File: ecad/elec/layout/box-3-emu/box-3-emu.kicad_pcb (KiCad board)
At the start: 2 copper layers, 72.5 x 63.9 mm, 56 parts

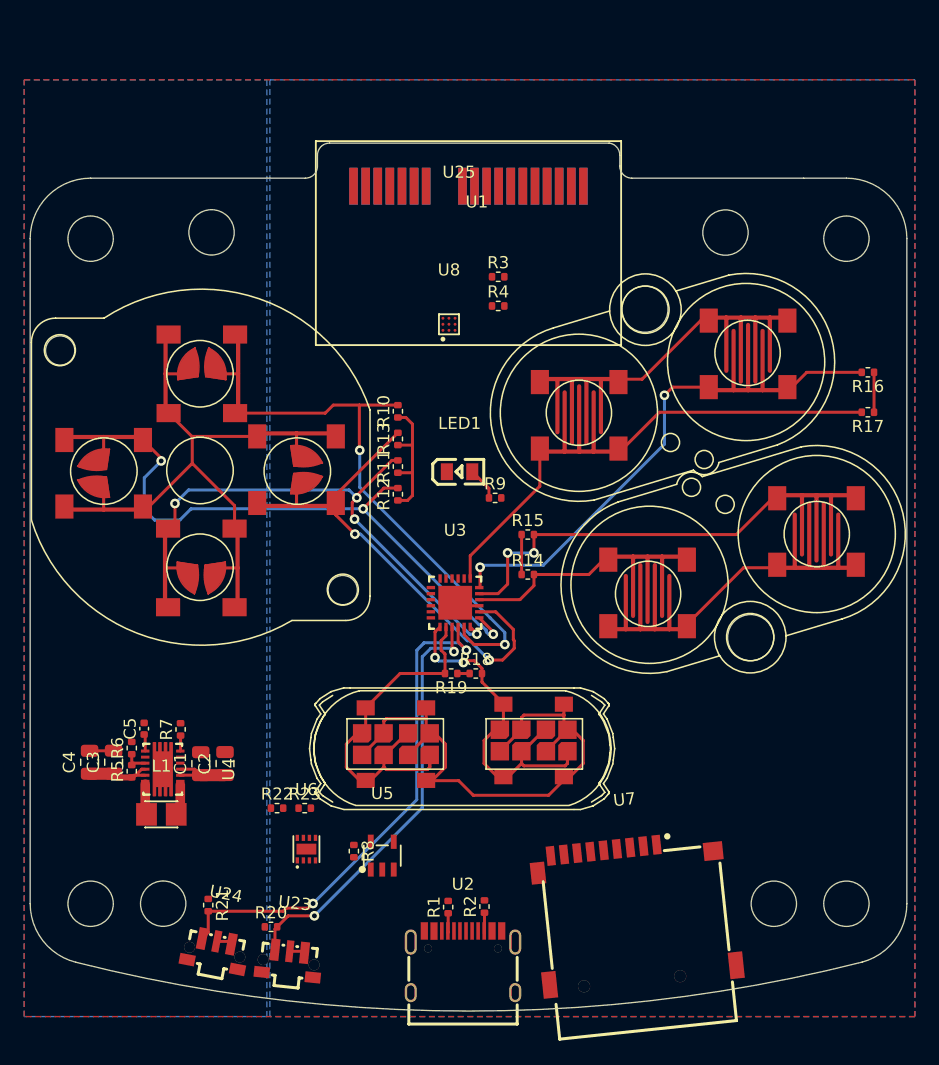
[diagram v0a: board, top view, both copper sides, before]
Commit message: update box-emu and box-3-emu borads
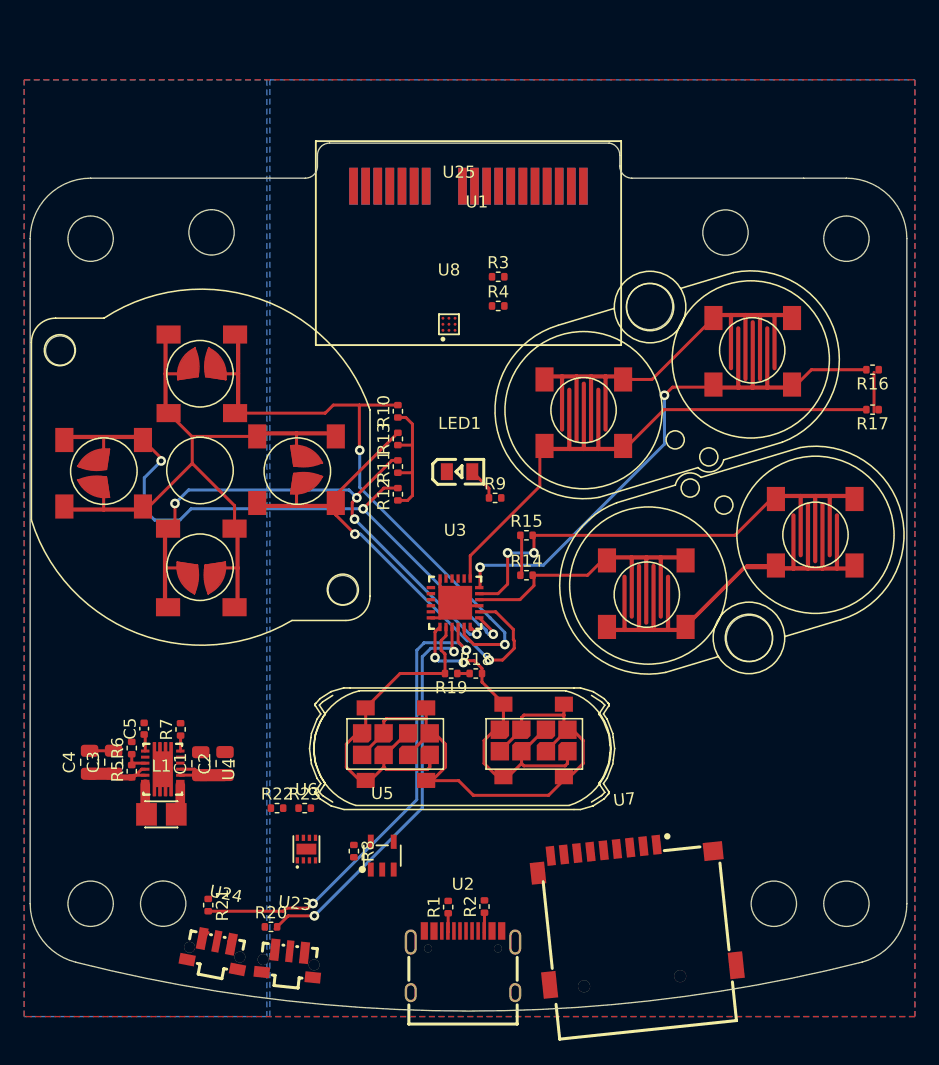
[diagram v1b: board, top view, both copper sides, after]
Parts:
- moved R16 0.44 mm to (168.9, 73.9)
- moved R17 0.44 mm to (168.9, 77.2)
- moved U18 0.44 mm to (159.0, 72.3)
- moved U19 0.44 mm to (145.0, 77.4)
- moved U17 0.44 mm to (152.0, 74.7)
- moved R14 0.12 mm to (140.3, 90.8)
- moved R15 0.12 mm to (140.3, 87.5)
- moved U14 0.12 mm to (157.2, 90.0)
- moved U15 0.12 mm to (150.2, 92.4)
- moved U16 0.12 mm to (164.1, 87.3)
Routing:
- net box-vcc: track 50.9 -> 67.8 mm
- net (no net): track 12.5 -> 0.00 mm
- net box-gnd: track 22.8 -> 27.9 mm
- net p1_3: track 42.7 -> 41.0 mm
- net p1_2: track 35.7 -> 34.0 mm

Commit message: WIP fleshing out more of the design
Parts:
- added U2: , lib:CONN-SMD_P2.00_S2B-PH-SM4-TB-LF-SN, B.Cu at (119.6, 116.7)
- R6: value 62.5mW Thick Film Resistors 50V ±100ppm/℃ ±0.5% 27.4kΩ 0402 Chip Resistor - Surface Mount ROHS -> 62.5mW Thick Film Resistors 50V ±100ppm/℃ ±1% 27.4kΩ 0402 Chip Resistor - Surface Mount ROHS
- renumbered U9 to U10, U10 to U11, U11 to U12, U12 to U13, U13 to U14, U14 to U15, U15 to U16, U16 to U17, U17 to U18, U18 to U19, U19 to U20, U20 to U21, U21 to U22, U22 to U23, U23 to U24, U24 to U25, U25 to U26, U26 to U27, U2 to U3, U3 to U4, U4 to U5, U5 to U6, U6 to U7, U7 to U8, U8 to U9
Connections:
- U24 pad 1: p1_2 -> box-vcc
- U24 pad 2: box-vcc -> p1_2
- U25 pad 1: p1_3 -> box-vcc
- U25 pad 2: box-vcc -> p1_3
- U4 pad 18: ad0 -> box-gnd
- U4 pad 24: ad1 -> box-gnd
- U9 pad A1: (no net) -> en
- U9 pad A2: (no net) -> reg
- U9 pad A3: (no net) -> out_p
- U9 pad B1: (no net) -> in_trig
- U9 pad B2: (no net) -> sda
- U9 pad B3: (no net) -> box-gnd
- U9 pad C1: (no net) -> scl
- U9 pad C2: (no net) -> box-vcc
- U9 pad C3: (no net) -> out_m
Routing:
- net p1_3: track 41.0 -> 40.3 mm
- net box-vcc: track 67.8 -> 68.5 mm

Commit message: update layouts
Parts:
- removed the U27 at (135.5, 58.7)
- added DS1: , lib:SOD-323_L1.8-W1.3-LS2.5-RD, F.Cu at (118.7, 103.5)
- added J1: , lib:CONN-SMD_4P-P1.00_SM04B-SRSS-TB-LF-SN, F.Cu at (165.7, 105.3)
- added U10: , Connector_PinHeader_1.00mm:PinHeader_1x02_P1.00mm_Vertical, F.Cu at (125.0, 65.4)
- added U28: , lib:CONN_5-1734857-1_TEC, F.Cu at (135.5, 58.7)
- moved U2 6.09 mm to (125.2, 119.1)
- renumbered U10 to U11, U11 to U12, U12 to U13, U13 to U14, U14 to U15, U15 to U16, U16 to U17, U17 to U18, U18 to U19, U19 to U20, U20 to U21, U21 to U22, U22 to U23, U23 to U24, U24 to U25, U25 to U26, U26 to U27
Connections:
- U9 pad A3: out_p -> a
- U9 pad C3: out_m -> b

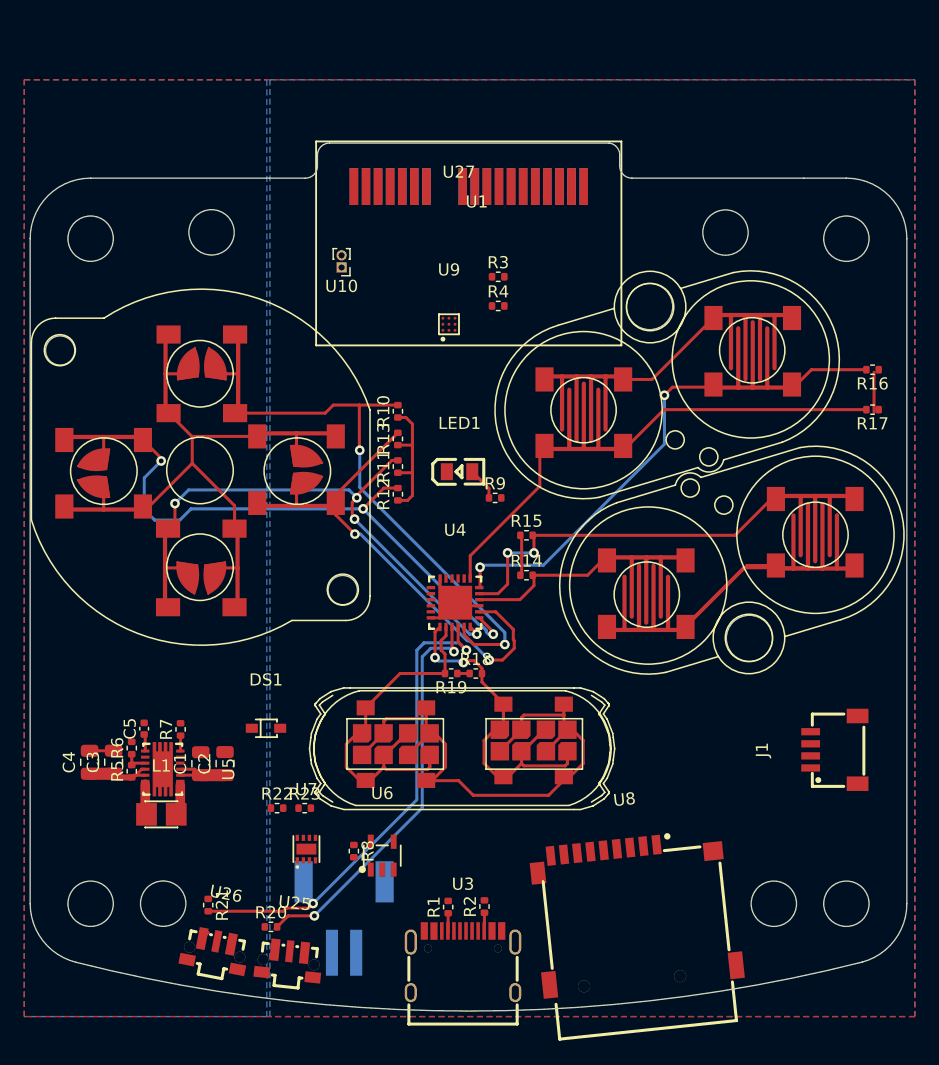
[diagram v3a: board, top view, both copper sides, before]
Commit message: change drv2605 to tssop and update box-3 connector. flesh out implemenation and wiring
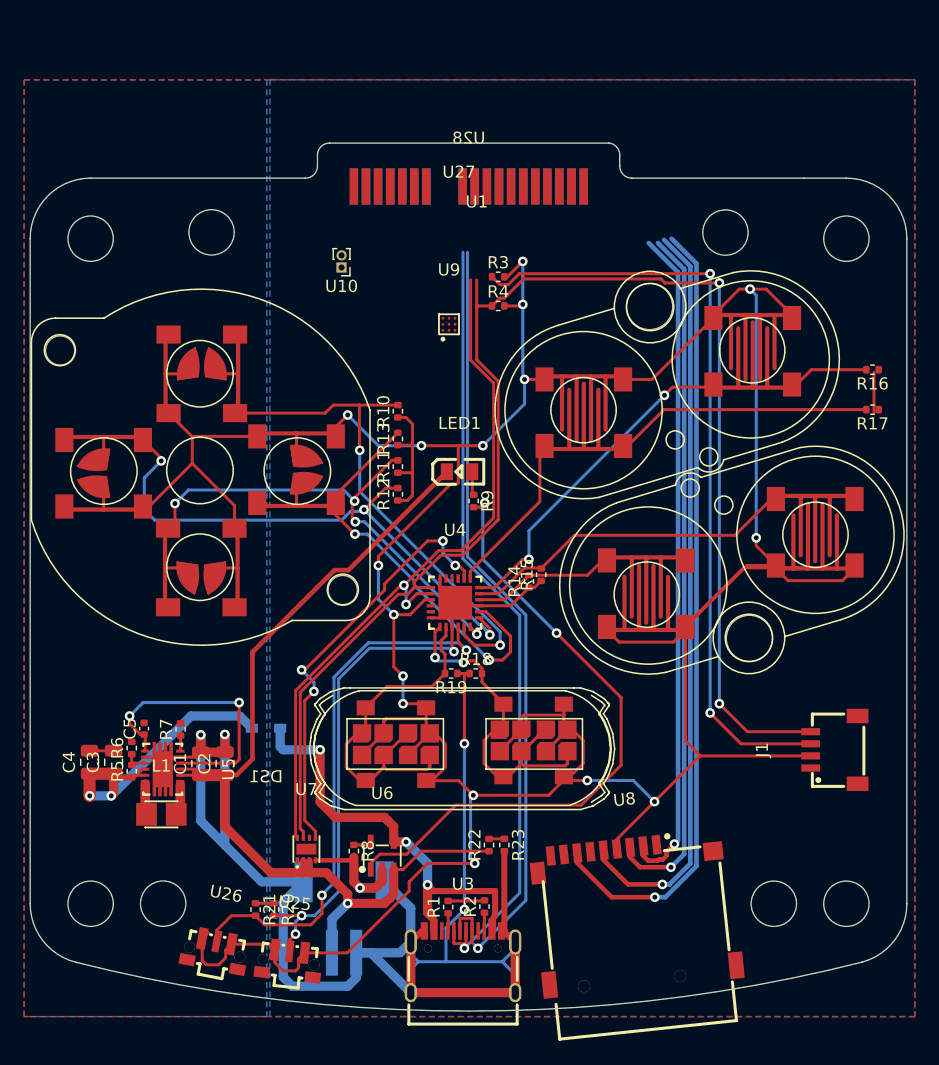
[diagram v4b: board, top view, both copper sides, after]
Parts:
- DS1: moved to B.Cu
- U28: footprint lib:CONN_5-1734857-1_TEC -> lib:CONN-SMD_5-1734857-1; moved to B.Cu
- moved R22 17.8 mm to (137.2, 113.2), turned to 90 degrees
- moved R23 16.8 mm to (138.4, 113.2), turned to -90 degrees
- moved R21 3.93 mm to (117.9, 118.5)
- moved R15 3.48 mm to (141.5, 90.8), turned to 90 degrees
- moved R9 1.79 mm to (135.9, 84.7), turned to -90 degrees
- moved R20 1.46 mm to (119.4, 118.5), turned to -90 degrees
- moved R14 0.55 mm to (140.5, 91.4), turned to 90 degrees
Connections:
- U28 pad A13: (no net) -> net-1
- U28 pad A15: (no net) -> net-2
- U28 pad B13: (no net) -> net-3
- U28 pad B15: (no net) -> net-4
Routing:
- net box-vcc: track 68.5 -> 260.7 mm, vias 0 -> 16
- net box-gnd: track 27.9 -> 172.8 mm, vias 0 -> 5
- net sda: track 0.00 -> 123.5 mm, vias 0 -> 4
- net scl: track 0.00 -> 121.1 mm, vias 0 -> 2
- net box-vcc-2: track 5.63 -> 78.5 mm, vias 0 -> 1
- net dp: track 0.00 -> 65.9 mm, vias 0 -> 1
- net miso: track 0.00 -> 65.7 mm, vias 0 -> 1
- net dm: track 0.00 -> 64.9 mm, vias 0 -> 1
- net sck: track 0.00 -> 62.0 mm, vias 0 -> 1
- net mosi: track 0.00 -> 57.5 mm, vias 0 -> 1
- net io42: track 0.00 -> 55.1 mm, vias 0 -> 3
- net cs: track 0.00 -> 55.1 mm, vias 0 -> 1
- net box.mcp73831-gnd: track 0.00 -> 52.1 mm, vias 0 -> 2
- net box-vcc-3: track 0.00 -> 38.4 mm, vias 0 -> 3
- net p1_4: track 0.00 -> 35.4 mm, vias 0 -> 4
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- added copper zone on F.Cu, net box-gnd
- added copper zone on B.Cu, net box-vcc
- removed copper zone on F.Cu, net (none)

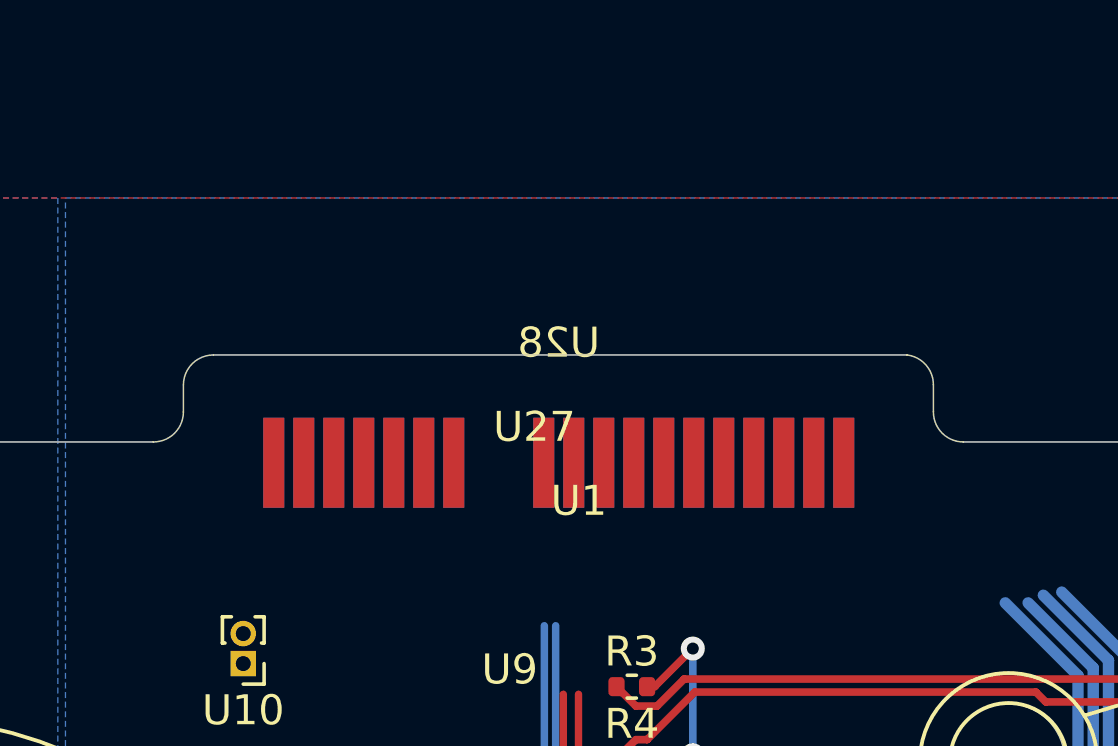
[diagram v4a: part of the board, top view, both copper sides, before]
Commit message: fix box-3 connector pin configuration (lcsc / easyeda model was wrong). updated associated layouts
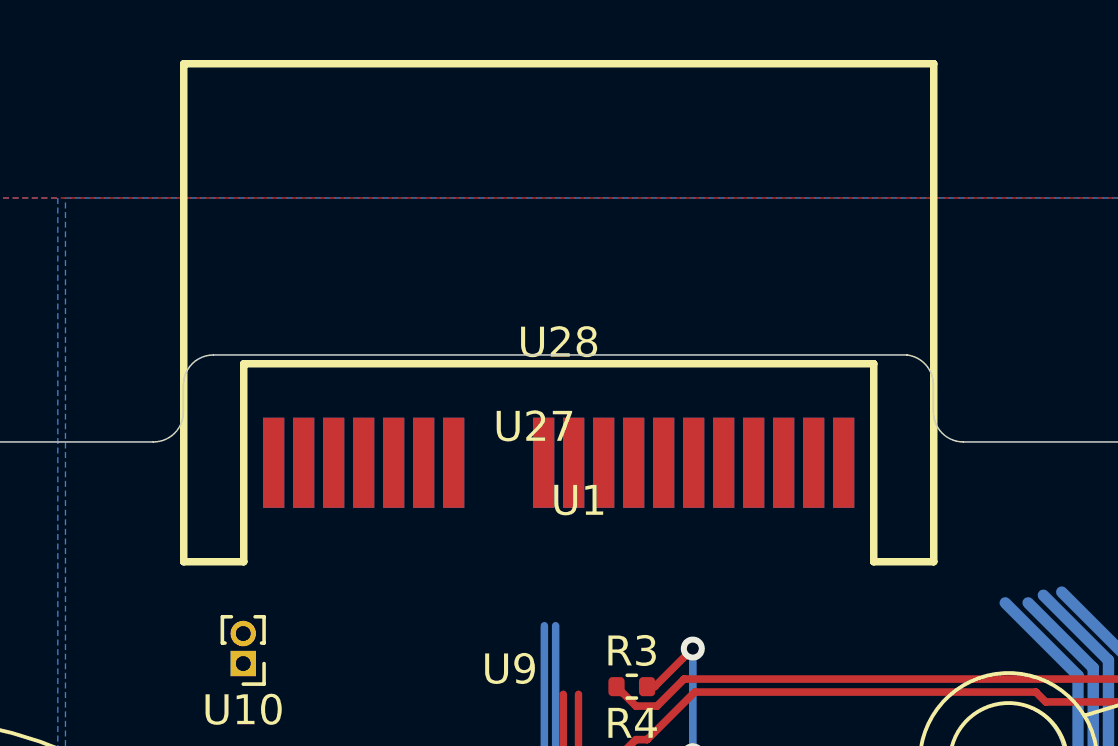
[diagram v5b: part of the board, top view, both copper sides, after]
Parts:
- U28: moved to F.Cu
- turned U28 to 0 degrees

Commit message: WIP layout
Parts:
- removed the R20 at (119.4, 118.5)
- added R10: 62.5mW Thick Film Resistors 50V ±100ppm/℃ ±1% 10kΩ 0402 Chi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, lib:R0402, F.Cu at (130.1, 61.6)
- added R22: 62.5mW Thick Film Resistors 50V ±100ppm/℃ ±1% 10kΩ 0402 Chi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, lib:R0402, F.Cu at (117.6, 118.5)
- U9: footprint lib:DSBGA-9_L1.5-W1.5-R3-C3-P0.50-BL -> lib:VSSOP-10_L3.0-W3.0-P0.50-LS4.9-BL
- moved U9 6.44 mm to (130.0, 64.9), turned to 90 degrees
- moved R21 1.27 mm to (119.1, 118.5)
- moved U10 1.01 mm to (125.0, 64.4), turned to 0 degrees
- moved U25 0.18 mm to (120.4, 123.0)
- moved U26 0.07 mm to (114.4, 122.1), turned to -10 degrees
- renumbered R10 to R11, R11 to R12, R12 to R13, R13 to R14, R14 to R15, R15 to R16, R16 to R17, R17 to R18, R18 to R19, R19 to R20, R22 to R23, R23 to R24
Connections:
- R21 pad 2: p1_3 -> p1_2
- U25 pad 4: box.vol_up.btn.btn-_4 -> box-gnd
- U25 pad 5: box.vol_up.btn.btn-_4 -> box-gnd
- U26 pad 4: box.vol_down.btn.btn-_4 -> box-gnd
- U26 pad 5: box.vol_down.btn.btn-_4 -> box-gnd
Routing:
- net box-gnd: track 172.8 -> 319.9 mm, vias 5 -> 12
- net io42: track 55.1 -> 0.00 mm, vias 3 -> 0
- net p1_2: track 0.00 -> 39.9 mm
- net box-vcc: track 260.7 -> 287.6 mm
- net scl: track 121.1 -> 139.9 mm, vias 2 -> 6
- net sda: track 123.5 -> 141.8 mm, vias 4 -> 7
- net miso: track 65.7 -> 79.3 mm, vias 1 -> 2
- net sck: track 62.0 -> 74.5 mm
- net cs: track 55.1 -> 63.2 mm, vias 1 -> 2
- net mosi: track 57.5 -> 65.6 mm
- net en: track 0.00 -> 3.06 mm
- net b: track 0.00 -> 2.73 mm
- net a: track 0.00 -> 2.73 mm
- net p1_4: track 35.4 -> 36.7 mm
- net box.mcp73831-gnd: track 52.1 -> 53.0 mm
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- added copper zone on B.Cu, net box-gnd
- removed copper zone on B.Cu, net box-vcc

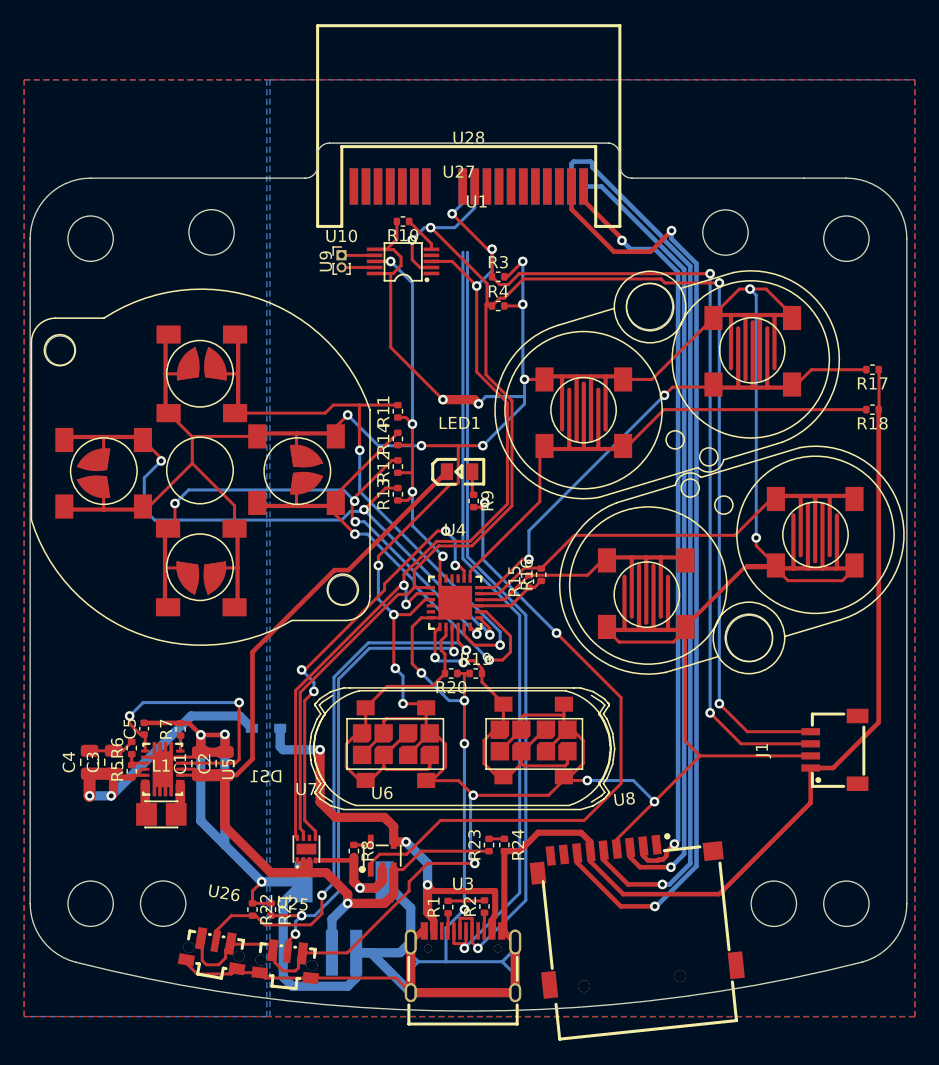
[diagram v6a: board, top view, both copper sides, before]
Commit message: fleshing out routing for base, box, and box-3
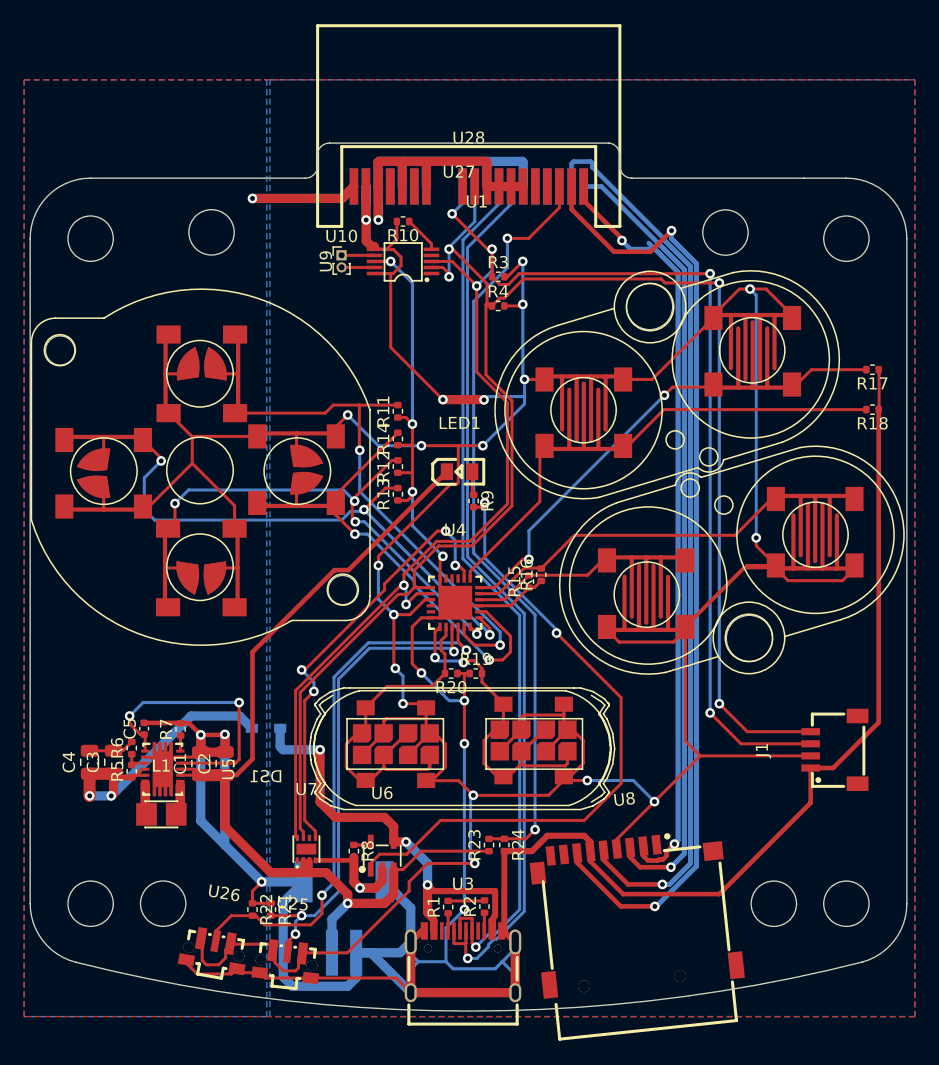
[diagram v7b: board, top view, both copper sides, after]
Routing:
- net battery_measurement: track 1.27 -> 63.4 mm, vias 0 -> 2
- net miso: track 79.3 -> 136.8 mm
- net sck: track 74.5 -> 130.0 mm
- net mosi: track 65.6 -> 118.5 mm
- net cs: track 63.2 -> 114.0 mm
- net box-gnd: track 319.9 -> 368.3 mm, vias 12 -> 13
- net box-vcc-1: track 26.5 -> 44.1 mm, vias 2 -> 3
- net dm: track 64.9 -> 74.1 mm
- net box-vcc: track 287.6 -> 295.5 mm, vias 16 -> 19
- net dp: track 65.9 -> 72.4 mm
- net scl: track 139.9 -> 136.4 mm, vias 6 -> 4
- net p1_2: vias 0 -> 3
- net box.max17048-ep: vias 3 -> 0
- added copper zone on B.Cu, net box-vcc
- added copper zone on B.Cu, net box-vcc-1
- removed copper zone on B.Cu, net (none)
- removed copper zone on B.Cu, net box-gnd
